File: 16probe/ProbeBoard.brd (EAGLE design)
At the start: 63.5 x 13 mm, 84 parts, among them Q1 2N7002, Q2 2N7002, U1 LTC2495CUHFPBF, U3 MAX6037AAUKADJ+T, U4 CSTCE16M0V53A-R0, U5 TPS79733DCKR, U6 ATMEGA328P_TQFPQFN_32

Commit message: signal traces for 16 probe board
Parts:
- removed R27: 2.2k, SparkFun:0603-RES
- removed TEMP16, TEMP8-5V1: (no value), wirepad:1,6/0,9
- moved TEMP11 34.8 mm to (10.2, 3.17), flipped to the bottom
- moved TEMP9 33.9 mm to (14.0, 3.17)
- moved TEMP15 30.0 mm to (2.54, 3.17)
- moved TEMP14 29.4 mm to (4.45, 3.17)
- moved TEMP1 28.2 mm to (2.54, 9.53)
- moved TEMP13 27.3 mm to (6.35, 3.17)
- moved TEMP10 27.0 mm to (12.1, 3.17)
- moved TEMP12 24.8 mm to (8.26, 3.17)
- moved TEMP2 23.8 mm to (4.45, 9.53)
- moved TEMP3 19.5 mm to (6.35, 9.53)
- moved R21 17.6 mm to (19.1, 5.21)
- moved TEMP4 15.9 mm to (8.26, 9.53)
- moved R17 15.1 mm to (23.4, 6.43), turned to 180 degrees
- moved TEMP3-5V 15.0 mm to (6.40, -9.17)
- moved TEMP5-5V 14.4 mm to (8.94, -8.53)
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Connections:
- removed net CH15: R27.1, TEMP16.1, U1.23
- net +5V: no longer TEMP8-5V1.1
- net CH10: now also U1.19; no longer U1.18
- net CH11: now also U1.20; no longer U1.19
- net CH12: now also U1.21; no longer U1.20
- net CH13: now also U1.22; no longer U1.21
- net CH14: now also U1.23; no longer U1.22
- net CH8: now also U1.17
- net CH9: now also U1.18; no longer U1.17
- net COM: no longer R27.2
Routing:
- net CH11: track 0.00 -> 16.1 mm
- net CH12: track 1.20 -> 17.2 mm
- net CH15: track 15.1 -> 0.00 mm
- net +5V: track 108.6 -> 122.2 mm, vias 5 -> 7
- net CH10: track 0.00 -> 12.6 mm
- net CH8: track 0.00 -> 12.4 mm
- net CH13: track 5.97 -> 18.0 mm
- net CH14: track 9.76 -> 20.4 mm
- net CH9: track 0.50 -> 10.1 mm
- net VCC_READ: track 0.00 -> 6.88 mm
- net CH7: track 14.5 -> 12.6 mm
- net COM: track 30.2 -> 31.4 mm, vias 8 -> 11
- net CH6: track 13.3 -> 12.7 mm
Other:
- board text added: "v0.1 (15)"
- board text removed: "v0.1 (16)"

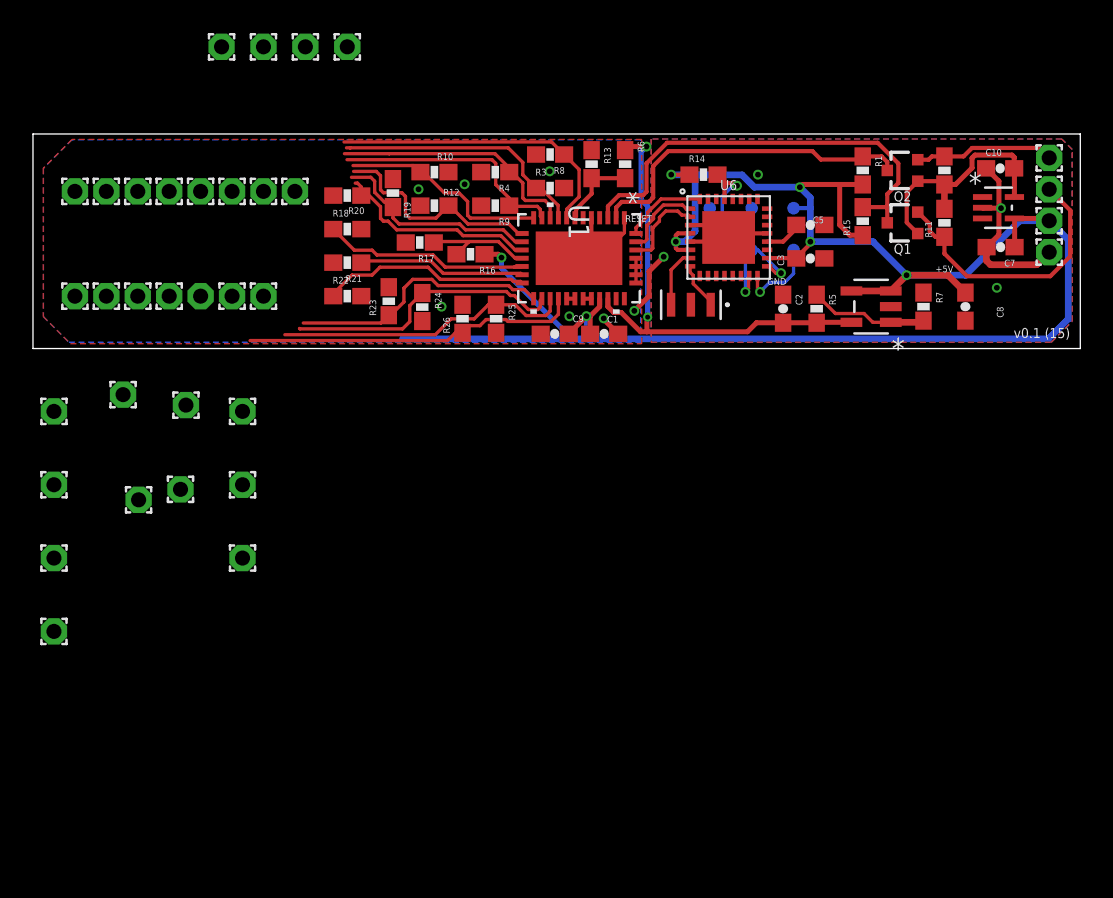
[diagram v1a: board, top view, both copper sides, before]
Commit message: probe pad placement, silkscreen
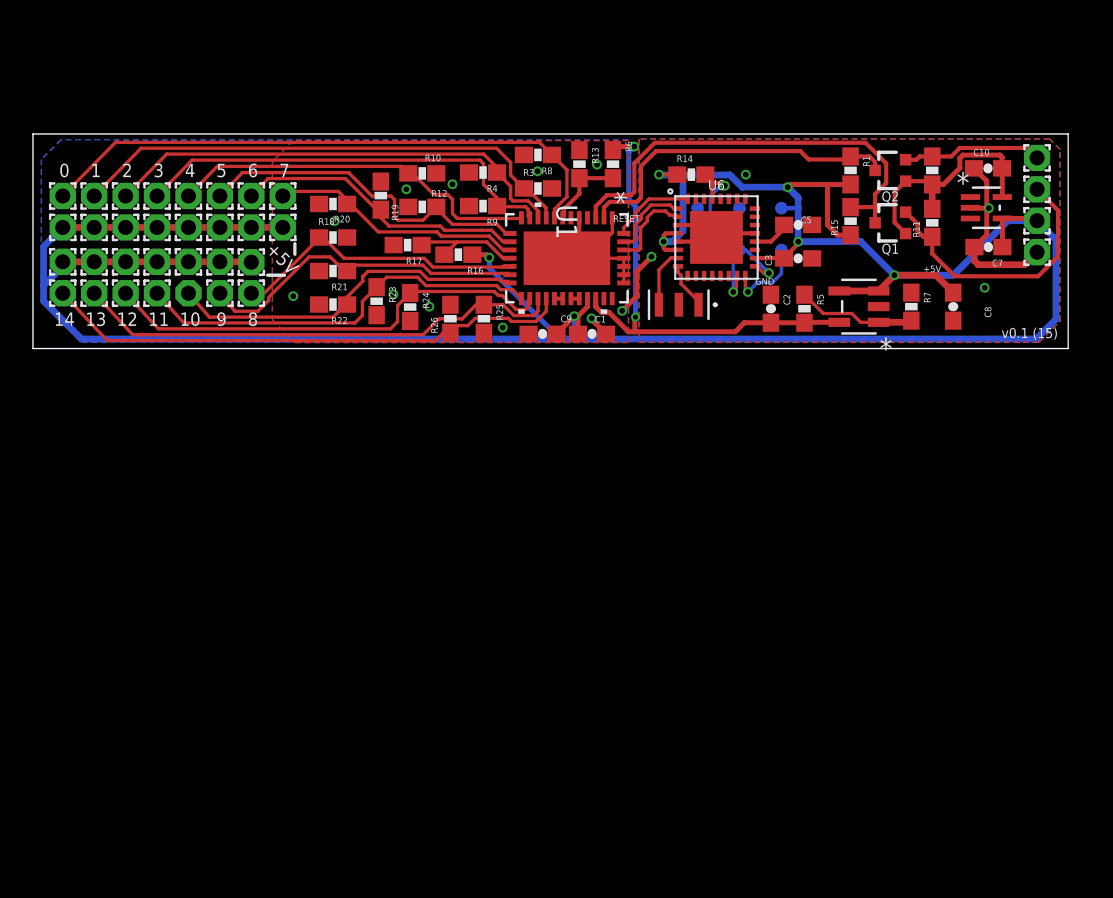
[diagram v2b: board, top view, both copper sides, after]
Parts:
- moved TEMP7-5V1 24.6 mm to (11.3, 5.26)
- moved TEMP5-5V1 19.7 mm to (9.42, 5.26)
- moved TEMP6-5V1 18.7 mm to (7.52, 5.26)
- moved TEMP3-5V1 18.0 mm to (13.2, 5.23)
- moved TEMP4-5V1 15.8 mm to (15.1, 7.34)
- moved TEMP5-5V 14.8 mm to (3.71, 5.26)
- moved TEMP7-5V 14.6 mm to (9.42, 7.34)
- moved TEMP3-5V 14.4 mm to (5.61, 5.26)
- moved TEMP1-5V 14.2 mm to (7.52, 7.34)
- moved TEMP6-5V 13.8 mm to (5.61, 7.34)
- moved TEMP4-5V 13.4 mm to (3.71, 7.34)
- moved TEMP8-5V 11.5 mm to (13.2, 7.34)
- moved TEMP2-5V1 11.2 mm to (11.3, 7.34)
- moved TEMP2-5V 10.8 mm to (1.80, 7.34)
- moved TEMP1-5V1 9.08 mm to (1.80, 5.26)
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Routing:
- net +5V: track 122.2 -> 175.2 mm
- net CH0: track 18.2 -> 35.8 mm
- net CH1: track 15.5 -> 31.2 mm
- net CH2: track 15.2 -> 28.5 mm
- net CH13: track 18.0 -> 29.9 mm
- net CH14: track 20.4 -> 32.2 mm
- net CH3: track 14.5 -> 26.2 mm
- net CH12: track 17.2 -> 27.9 mm
- net CH9: track 10.1 -> 20.3 mm
- net CH4: track 12.8 -> 22.8 mm
- net COM: track 31.4 -> 40.7 mm, vias 11 -> 15
- net CH10: track 12.6 -> 22.0 mm
- net CH11: track 16.1 -> 25.1 mm
- net CH5: track 13.5 -> 21.0 mm
- net CH8: track 12.4 -> 17.9 mm
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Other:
- board size 63.5 x 13 mm -> 62.7 x 13 mm
- board text added: "0"
- board text added: "1"
- board text added: "10"
- board text added: "11"
- board text added: "12"
- board text added: "13"
- board text added: "14"
- board text added: "2"
- board text added: "3"
- board text added: "4"
- board text added: "5"
- board text added: "6"
- board text added: "7"
- board text added: "8"
- board text added: "9"
